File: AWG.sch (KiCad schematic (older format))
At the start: 0 parts

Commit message: Added Fast DAC schematic
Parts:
- added C?: C_Small, Capacitor_SMD:C_0603_1608Metric_Pad1.08x0.95mm_HandSolder, symbol Device:C_Small
- added C?: C_Polarized_Small, Capacitor_Tantalum_SMD:CP_EIA-1608-10_AVX-L_Pad1.25x1.05mm_HandSolder, symbol Device:C_Polarized_Small
- added C?: C_Small, symbol Device:C_Small
- added C? (x3): 100uF, Capacitor_Tantalum_SMD:CP_EIA-6032-28_Kemet-C, symbol Device:C_Polarized_Small
- added C? (x16): 100nF, Capacitor_SMD:C_0603_1608Metric_Pad1.08x0.95mm_HandSolder, symbol Device:C_Small
- added FB?: MPZ2012S601AT000, digikey-footprints:0805, symbol dk_Ferrite-Beads-and-Chips:MPZ2012S601AT000
- added IC?: AD9726BSVZ, QFP50P1400X1400X120-81N, symbol GM_DAC:AD9726BSVZ
- added L?: L_Small, symbol Device:L_Small
- added L? (x3): 10uH, Inductor_SMD:L_1210_3225Metric_Pad1.42x2.65mm_HandSolder, symbol Device:L_Small
- added R?: R_Small_US, Resistor_SMD:R_0603_1608Metric_Pad0.98x0.95mm_HandSolder, symbol Device:R_Small_US
- added R?: 1K, Resistor_SMD:R_0603_1608Metric_Pad0.98x0.95mm_HandSolder, symbol Device:R_Small_US
- added R?: 2K, Resistor_SMD:R_0603_1608Metric_Pad0.98x0.95mm_HandSolder, symbol Device:R_Small_US
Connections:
- new net: IC?.2 (REXT), R?.1
- new net: C?.1, IC?.59 (REFIO)
- new net: IC?.60 (FSADJ), R?.1
- new net AVDD2V5: C?.1, C?.1, C?.1, C?.1, C?.1, C?.1, C?.1, IC?.1 (CLKVDD_1), IC?.3 (CLKVDD_2), IC?.62 (ADVDD_1), IC?.64 (ACVDD_1), IC?.77 (ACVDD_2), IC?.79 (ADVDD_2), L?.1
- new net AVDD3V3: C?.1, C?.1, C?.1, C?.1, C?.1, C?.1, C?.1, C?.1, IC?.20 (DBVDD_1), IC?.30 (DBVDD_2), IC?.40 (DBVDD_3), IC?.66 (AVDD2_1), IC?.68 (AVDD1_1), IC?.73 (AVDD1_2), IC?.75 (AVDD2_2), L?.1
- new net DVDD2V5: C?.1, C?.1, C?.1, IC?.52 (DVDD_2), IC?.9 (DVDD_1), L?.1
- new net FDAC_CLK: IC?.56 (SCLK_(SYNCUPD))
- new net FDAC_CLKIN_N: IC?.6 (CLK-)
- new net FDAC_CLKIN_P: IC?.5 (CLK+)
- new net FDAC_CS: IC?.57 (CSB)
- new net FDAC_DB0_N: IC?.51 (DB0-)
- new net FDAC_DB0_P: IC?.50 (DB0+)
- new net FDAC_DB10_N: IC?.23 (DB10-)
- new net FDAC_DB10_P: IC?.22 (DB10+)
- new net FDAC_DB11_N: IC?.19 (DB11-)
- new net FDAC_DB11_P: IC?.18 (DB11+)
- new net FDAC_DB12_N: IC?.17 (DB12-)
- new net FDAC_DB12_P: IC?.16 (DB12+)
- new net FDAC_DB13_N: IC?.15 (DB13-)
- new net FDAC_DB13_P: IC?.14 (DB13+)
- new net FDAC_DB14_N: IC?.13 (DB14-)
- new net FDAC_DB14_P: IC?.12 (DB14+)
- new net FDAC_DB15_N: IC?.11 (DB15-)
- new net FDAC_DB15_P: IC?.10 (DB15+)
- new net FDAC_DB1_N: IC?.49 (DB1-)
- new net FDAC_DB1_P: IC?.48 (DB1+)
- new net FDAC_DB2_N: IC?.47 (DB2-)
- new net FDAC_DB2_P: IC?.46 (DB2+)
- new net FDAC_DB3_N: IC?.45 (DB3-)
- new net FDAC_DB3_P: IC?.44 (DB3+)
- new net FDAC_DB4_N: IC?.43 (DB4-)
- new net FDAC_DB4_P: IC?.42 (DB4+)
- new net FDAC_DB5_N: IC?.39 (DB5-)
- new net FDAC_DB5_P: IC?.38 (DB5+)
- new net FDAC_DB6_N: IC?.37 (DB6-)
- new net FDAC_DB6_P: IC?.36 (DB6+)
- new net FDAC_DB7_N: IC?.35 (DB7-)
- new net FDAC_DB7_P: IC?.34 (DB7+)
- new net FDAC_DB8_N: IC?.27 (DB8-)
- new net FDAC_DB8_P: IC?.26 (DB8+)
- new net FDAC_DB9_N: IC?.25 (DB9-)
- new net FDAC_DB9_P: IC?.24 (DB9+)
- new net FDAC_DCLK_IN_N: IC?.33 (DCLK_IN-)
- new net FDAC_DCLK_IN_P: IC?.32 (DCLK_IN+)
- new net FDAC_DCLK_OUT_N: IC?.29 (DCLK_OUT-)
- new net FDAC_DCLK_OUT_P: IC?.28 (DCLK_OUT+)
- new net FDAC_SDI: IC?.55 (SDIO)
- new net FDAC_SDO: IC?.54 (SDO_(SYNCALRM))
- new net GNDD: C?.2, C?.2, C?.2, C?.2, C?.2, C?.2, C?.2, C?.2, C?.2, C?.2, C?.2, C?.2, C?.2, C?.2, C?.2, C?.2, C?.2, C?.2, C?.2, IC?.21 (DBGND_1), IC?.31 (DBGND_2), IC?.4 (CLKGND_1), IC?.41 (DBGND_3), IC?.53 (DGND_2), IC?.61 (SDR_EN), IC?.63 (ADGND_1), IC?.65 (ACGND_1), IC?.67 (AGND2_1), IC?.69 (AGND1_1), IC?.7 (CLKGND_2), IC?.72 (AGND1_2), IC?.74 (AGND2_2), IC?.76 (ACGND_2), IC?.78 (ADGND_2), IC?.8 (DGND_1), IC?.80 (SPI_DIS), IC?.81 (TH_PAD), R?.2, R?.2
- new net VCC2V5: L?.2, L?.2
- new net VCC3V3: L?.2
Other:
- note added: "Analog output circuit"
- note added: "Connect to FPGA"
- note added: "Connect to external clock generator in digital board\nNOTE - The CLK+ and CLK– input pins should be driven by a signal\nwith a common-mode voltage near ½ of CLKVDD"

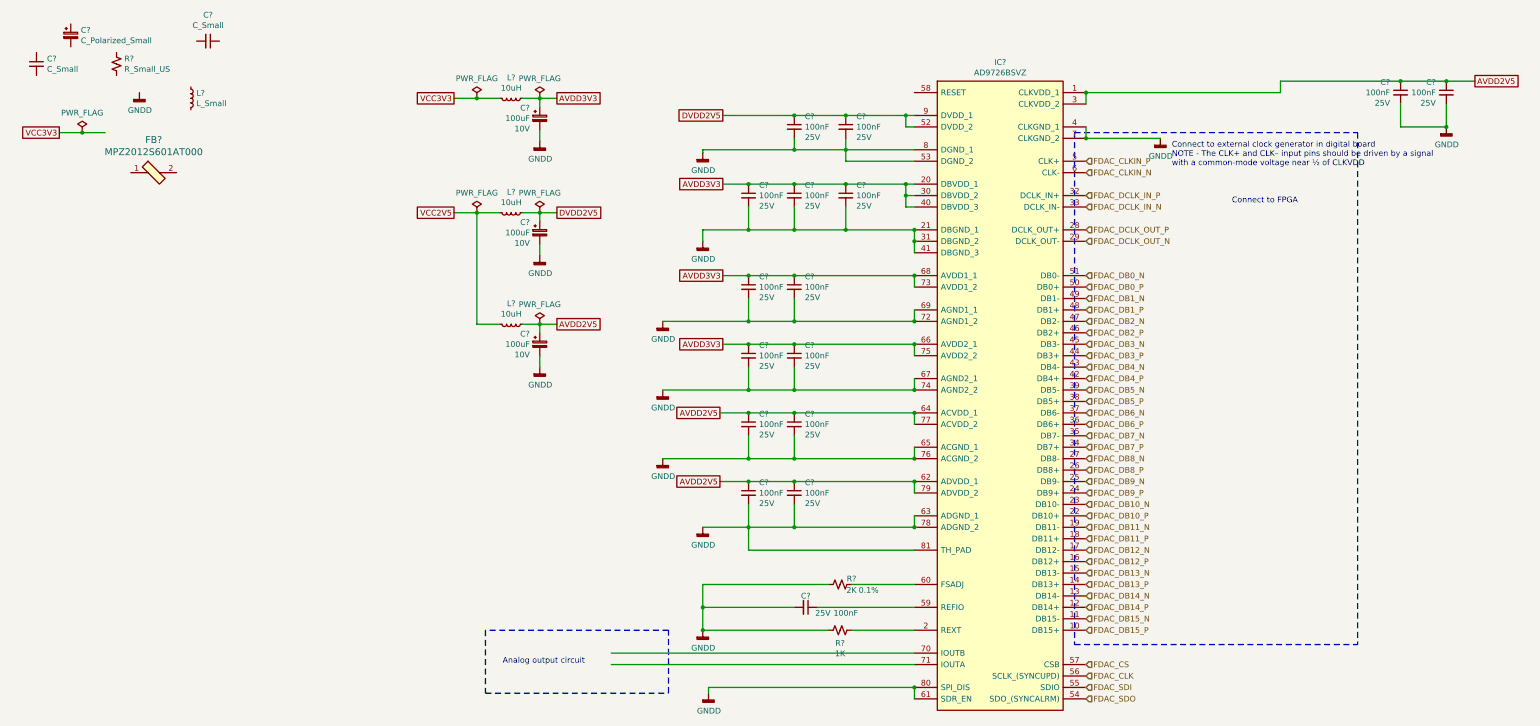
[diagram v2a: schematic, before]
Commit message: PCB created and schematics annotated High speed connections added to the BTB
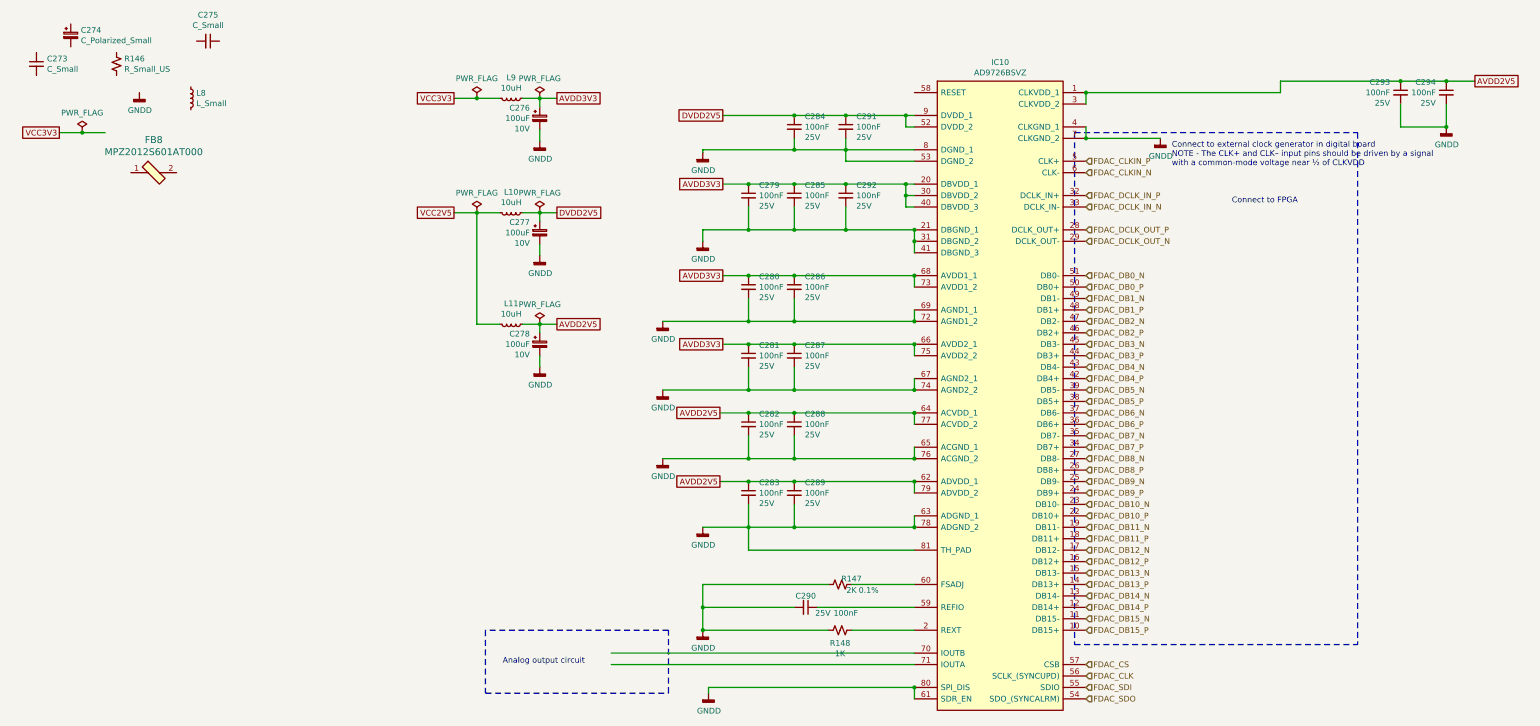
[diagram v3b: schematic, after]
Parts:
- gave numbers to parts that had none: 31

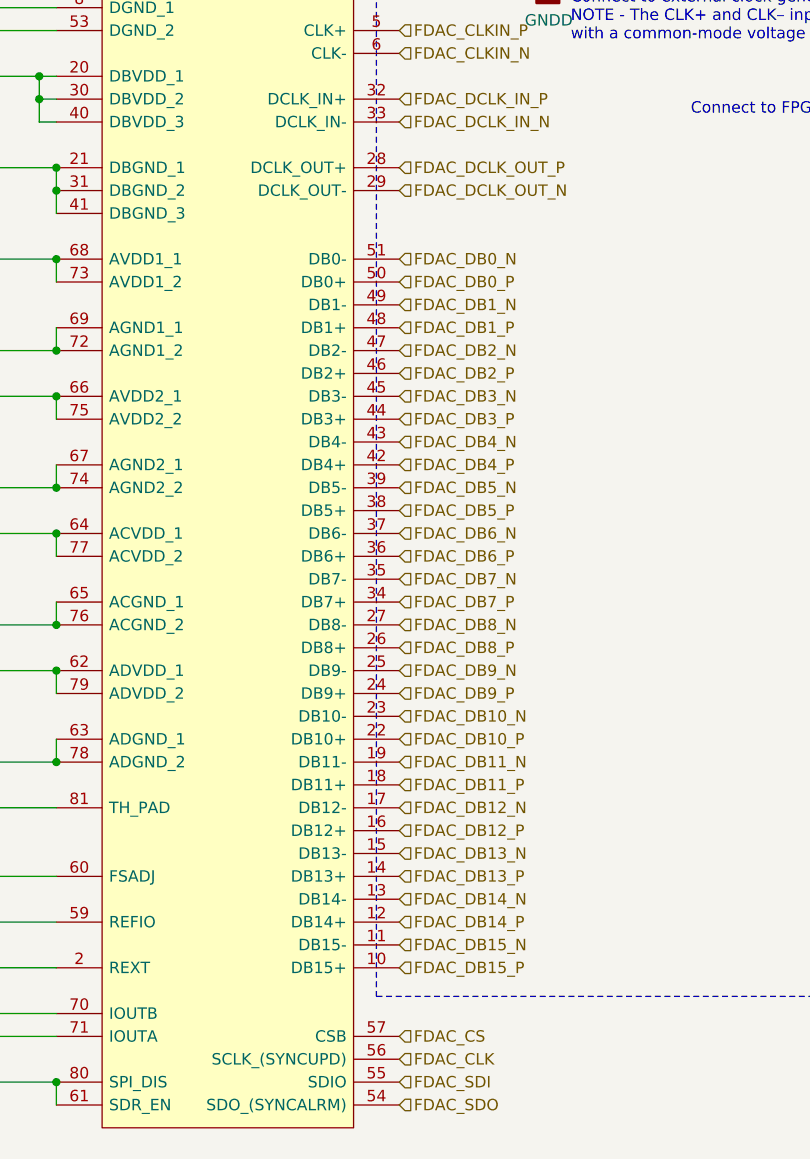
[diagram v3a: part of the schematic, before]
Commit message: BTB and FPGA pins added and connections were made
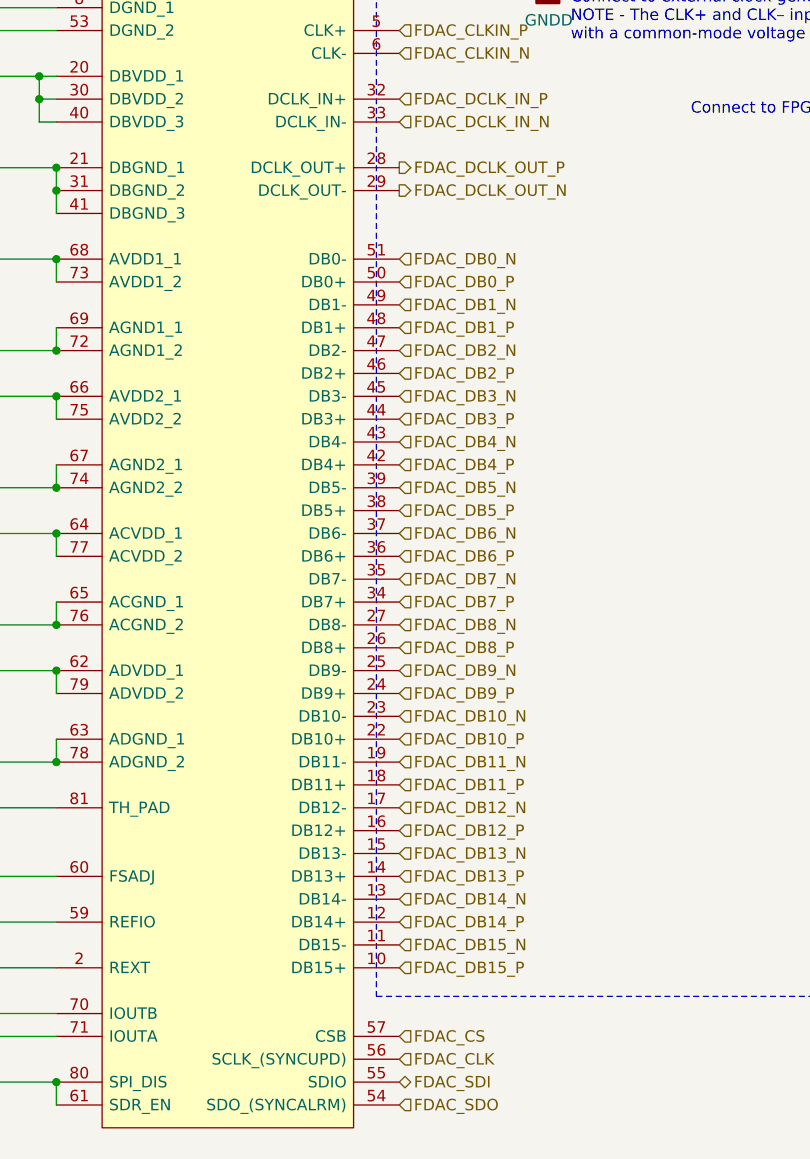
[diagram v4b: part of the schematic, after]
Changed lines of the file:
@@
 Text Notes 7550 1500 0    50   ~ 0
 Connect to external clock generator in digital board\nNOTE - The CLK+ and CLK– input pins should be driven by a signal\nwith a common-mode voltage near ½ of CLKVDD
-Text HLabel 6800 2050 2    50   Input ~ 0
+Text HLabel 6800 2050 2    50   Output ~ 0
 FDAC_DCLK_OUT_P
-Text HLabel 6800 2150 2    50   Input ~ 0
+Text HLabel 6800 2150 2    50   Output ~ 0
 FDAC_DCLK_OUT_N
 Text HLabel 6800 2550 2    50   Input ~ 0
@@
 Text HLabel 6800 5950 2    50   Input ~ 0
 FDAC_CLK
-Text HLabel 6800 6050 2    50   Input ~ 0
+Text HLabel 6800 6050 2    50   BiDi ~ 0
 FDAC_SDI
 Text HLabel 6800 6150 2    50   Input ~ 0

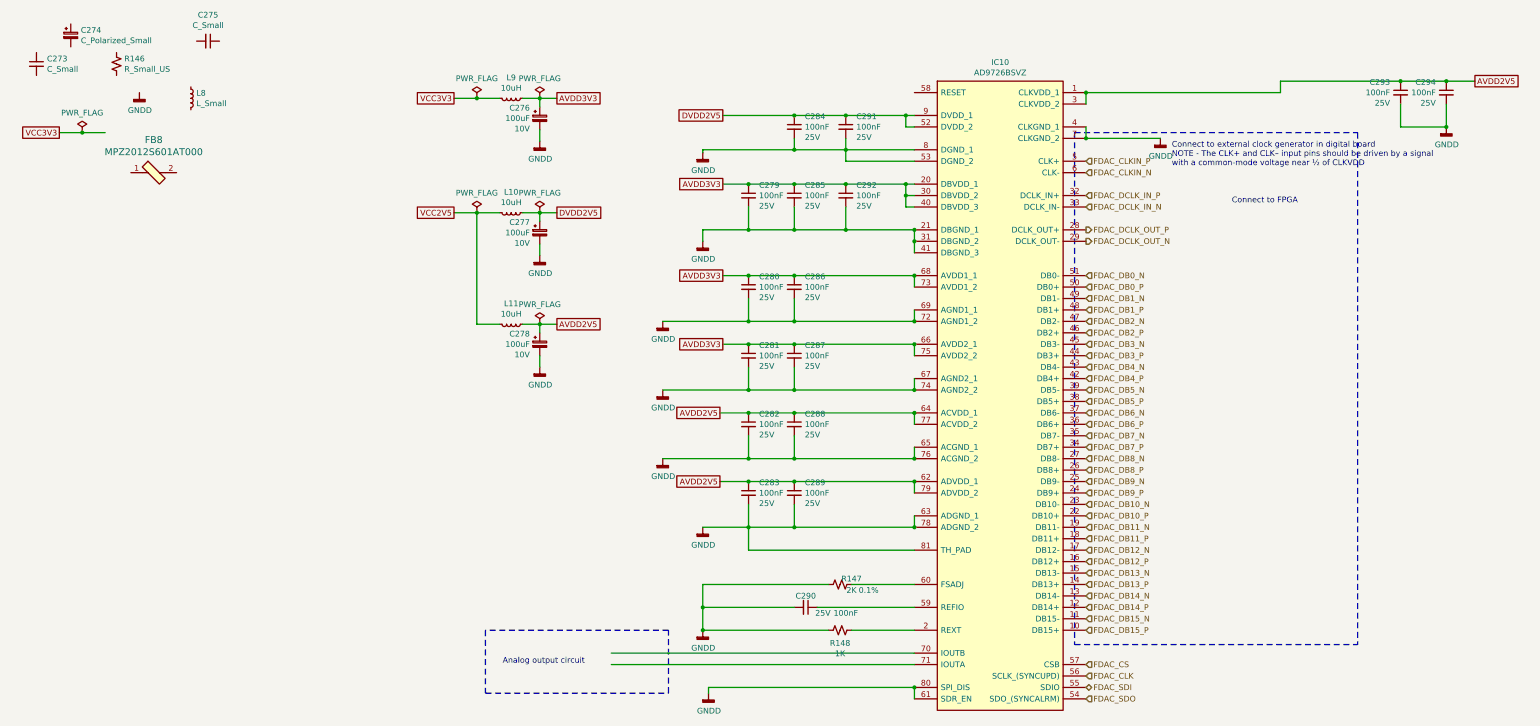
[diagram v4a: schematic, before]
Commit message: Corrected PCB import errors
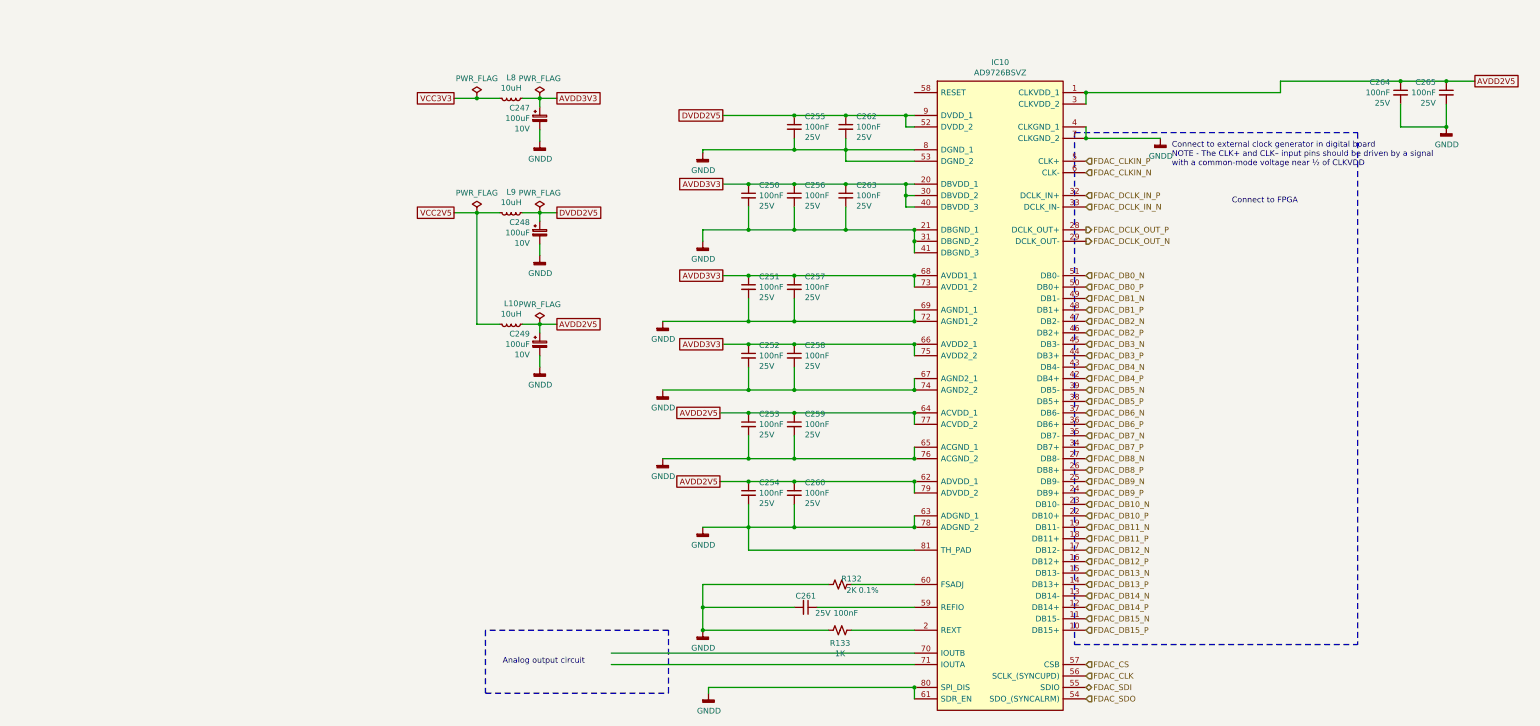
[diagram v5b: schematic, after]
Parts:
- removed C273: C_Small, Capacitor_SMD:C_0603_1608Metric_Pad1.08x0.95mm_HandSolder, symbol Device:C_Small
- removed C274: C_Polarized_Small, Capacitor_Tantalum_SMD:CP_EIA-1608-10_AVX-L_Pad1.25x1.05mm_HandSolder, symbol Device:C_Polarized_Small
- removed C275: C_Small, symbol Device:C_Small
- removed FB8: MPZ2012S601AT000, digikey-footprints:0805, symbol dk_Ferrite-Beads-and-Chips:MPZ2012S601AT000
- removed L8: L_Small, symbol Device:L_Small
- removed R146: R_Small_US, Resistor_SMD:R_0603_1608Metric_Pad0.98x0.95mm_HandSolder, symbol Device:R_Small_US
- renumbered C276 to C247, C277 to C248, C278 to C249, C279 to C250, C280 to C251, C281 to C252, C282 to C253, C283 to C254, C284 to C255, C285 to C256, C286 to C257, C287 to C258, C288 to C259, C289 to C260, C290 to C261, C291 to C262, C292 to C263, C293 to C264, C294 to C265, L11 to L10, L9 to L8, L10 to L9, R147 to R132, R148 to R133
